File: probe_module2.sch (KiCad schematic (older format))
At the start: 4 parts, among them J10 CONN_01X05, J9 CONN_01X05, U10 LH1526, U9 DG411

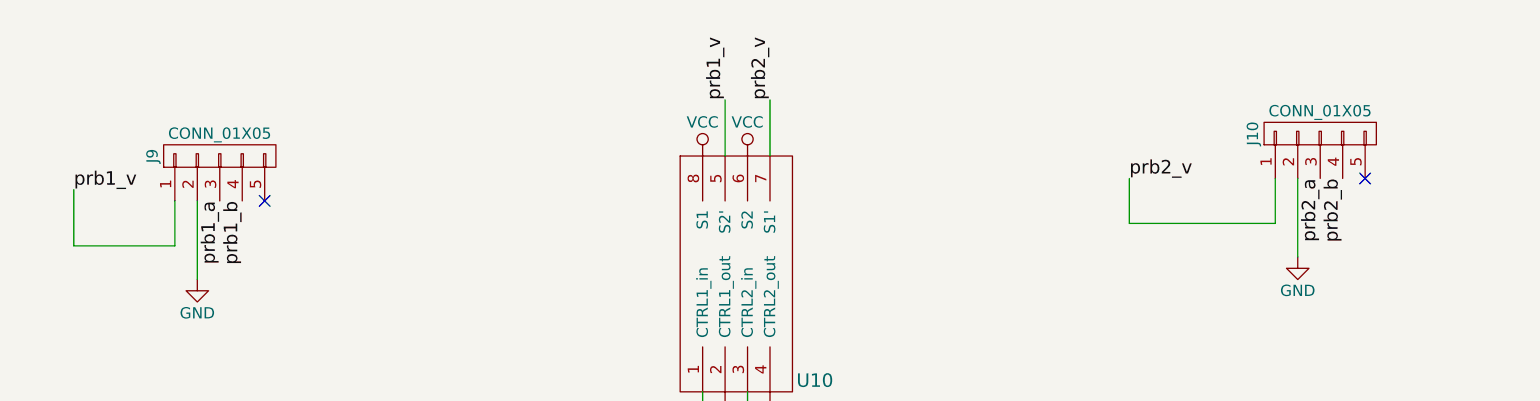
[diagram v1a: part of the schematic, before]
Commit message: add all the rest of the footprints
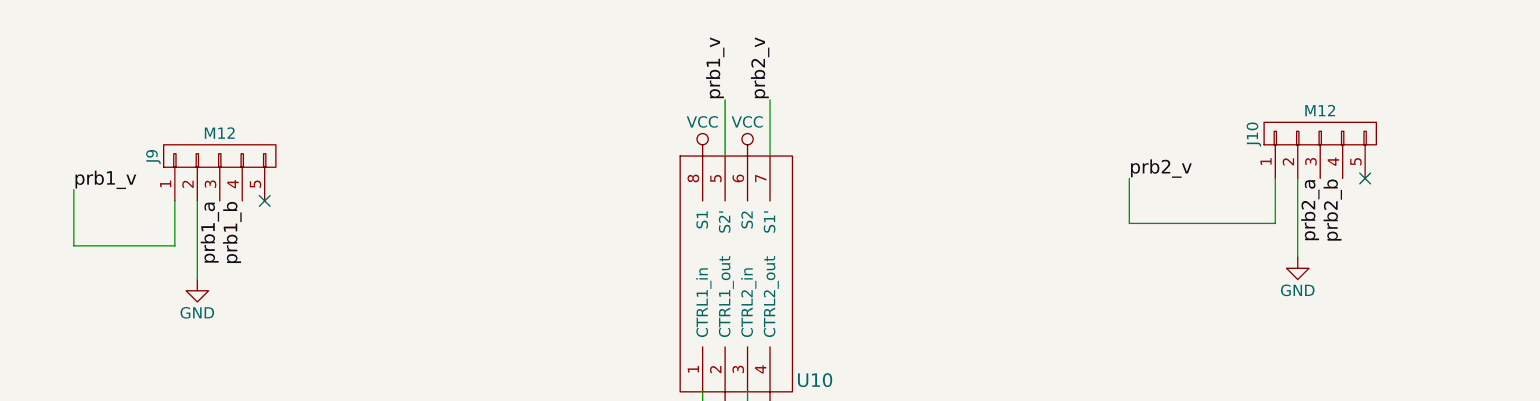
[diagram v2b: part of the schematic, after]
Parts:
- J10, J9: value CONN_01X05 -> M12; footprint (none) -> Connectors_Hirose:Hirose_DF13C-05P-1.25V_05x1.25mm_Straight
- U10: footprint (none) -> Housings_DIP:DIP-8_W9.53mm_SMD
- U9: footprint (none) -> Housings_SOIC:SOIC-8_3.9x4.9mm_Pitch1.27mm
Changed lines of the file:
@@
 F 0 "U9" H 2300 4550 50  0000 C CNN
 F 1 "DG411" H 2300 4350 50  0000 C CNN
-F 2 "" H 2300 4450 60  0001 C CNN
+F 2 "Housings_SOIC:SOIC-8_3.9x4.9mm_Pitch1.27mm" H 2300 4450 60  0001 C CNN
 F 3 "" H 2300 4450 60  0001 C CNN
 	1    2300 4450
@@
 F 0 "U9" H 4650 4550 50  0000 C CNN
 F 1 "DG411" H 4650 4350 50  0000 C CNN
-F 2 "" H 4650 4450 60  0001 C CNN
+F 2 "Housings_SOIC:SOIC-8_3.9x4.9mm_Pitch1.27mm" H 4650 4450 60  0001 C CNN
 F 3 "" H 4650 4450 60  0001 C CNN
 	2    4650 4450
@@
 F 0 "U9" H 7400 4550 50  0000 C CNN
 F 1 "DG411" H 7400 4350 50  0000 C CNN
-F 2 "" H 7400 4450 60  0001 C CNN
+F 2 "Housings_SOIC:SOIC-8_3.9x4.9mm_Pitch1.27mm" H 7400 4450 60  0001 C CNN
 F 3 "" H 7400 4450 60  0001 C CNN
 	3    7400 4450
@@
 F 0 "U9" H 9450 4500 50  0000 C CNN
 F 1 "DG411" H 9450 4300 50  0000 C CNN
-F 2 "" H 9450 4400 60  0001 C CNN
+F 2 "Housings_SOIC:SOIC-8_3.9x4.9mm_Pitch1.27mm" H 9450 4400 60  0001 C CNN
 F 3 "" H 9450 4400 60  0001 C CNN
 	4    9450 4400
@@
 P 3100 1700
 F 0 "J9" H 3100 2000 50  0000 C CNN
-F 1 "CONN_01X05" V 3200 1700 50  0000 C CNN
-F 2 "" H 3100 1700 50  0001 C CNN
+F 1 "M12" V 3200 1700 50  0000 C CNN
+F 2 "Connectors_Hirose:Hirose_DF13C-05P-1.25V_05x1.25mm_Straight" H 3100 1700 50  0001 C CNN
 F 3 "" H 3100 1700 50  0001 C CNN
 	1    3100 1700
@@
 P 8000 1600
 F 0 "J10" H 8000 1900 50  0000 C CNN
-F 1 "CONN_01X05" V 8100 1600 50  0000 C CNN
-F 2 "" H 8000 1600 50  0001 C CNN
+F 1 "M12" V 8100 1600 50  0000 C CNN
+F 2 "Connectors_Hirose:Hirose_DF13C-05P-1.25V_05x1.25mm_Straight" H 8000 1600 50  0001 C CNN
 F 3 "" H 8000 1600 50  0001 C CNN
 	1    8000 1600
@@
 F 0 "U10" H 5750 2900 60  0000 C CNN
 F 1 "LH1526" H 5750 2750 60  0000 C CNN
-F 2 "" H 5750 2750 60  0001 C CNN
+F 2 "Housings_DIP:DIP-8_W9.53mm_SMD" H 5750 2750 60  0001 C CNN
 F 3 "" H 5750 2750 60  0001 C CNN
 	1    5700 2800
